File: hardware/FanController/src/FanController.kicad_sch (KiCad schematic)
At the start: 11 parts, among them J1 Conn_01x02_Socket, J2 Fan_4pin, J3 Fan_4pin, J4 Fan_4pin, J5 Fan_4pin, U1 PIC12F1501-xMC, U2 MCP9700Ax-ETT

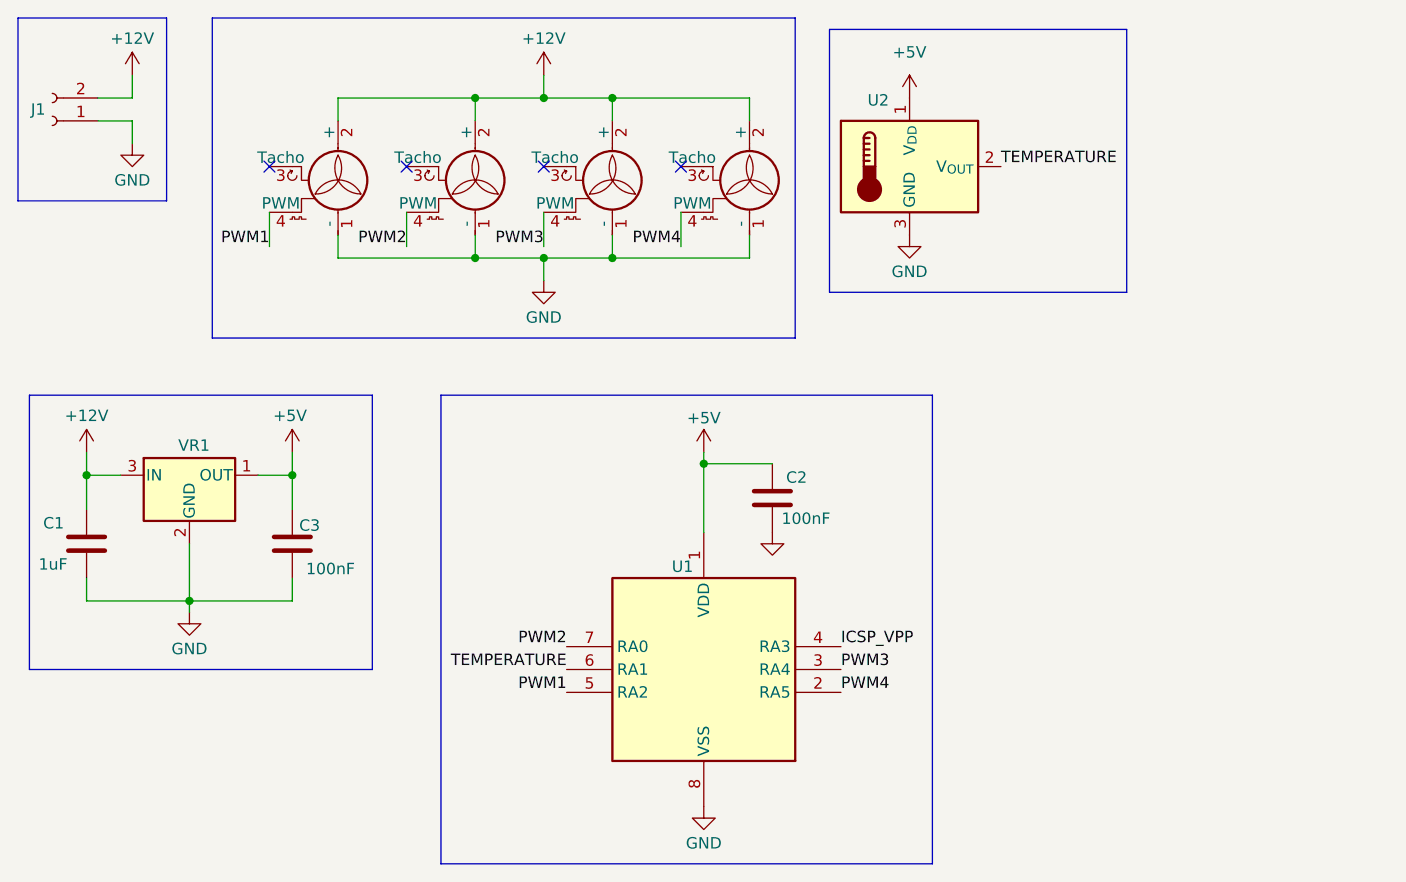
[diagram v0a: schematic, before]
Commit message: Replaced MCP9700A with MCP9701A
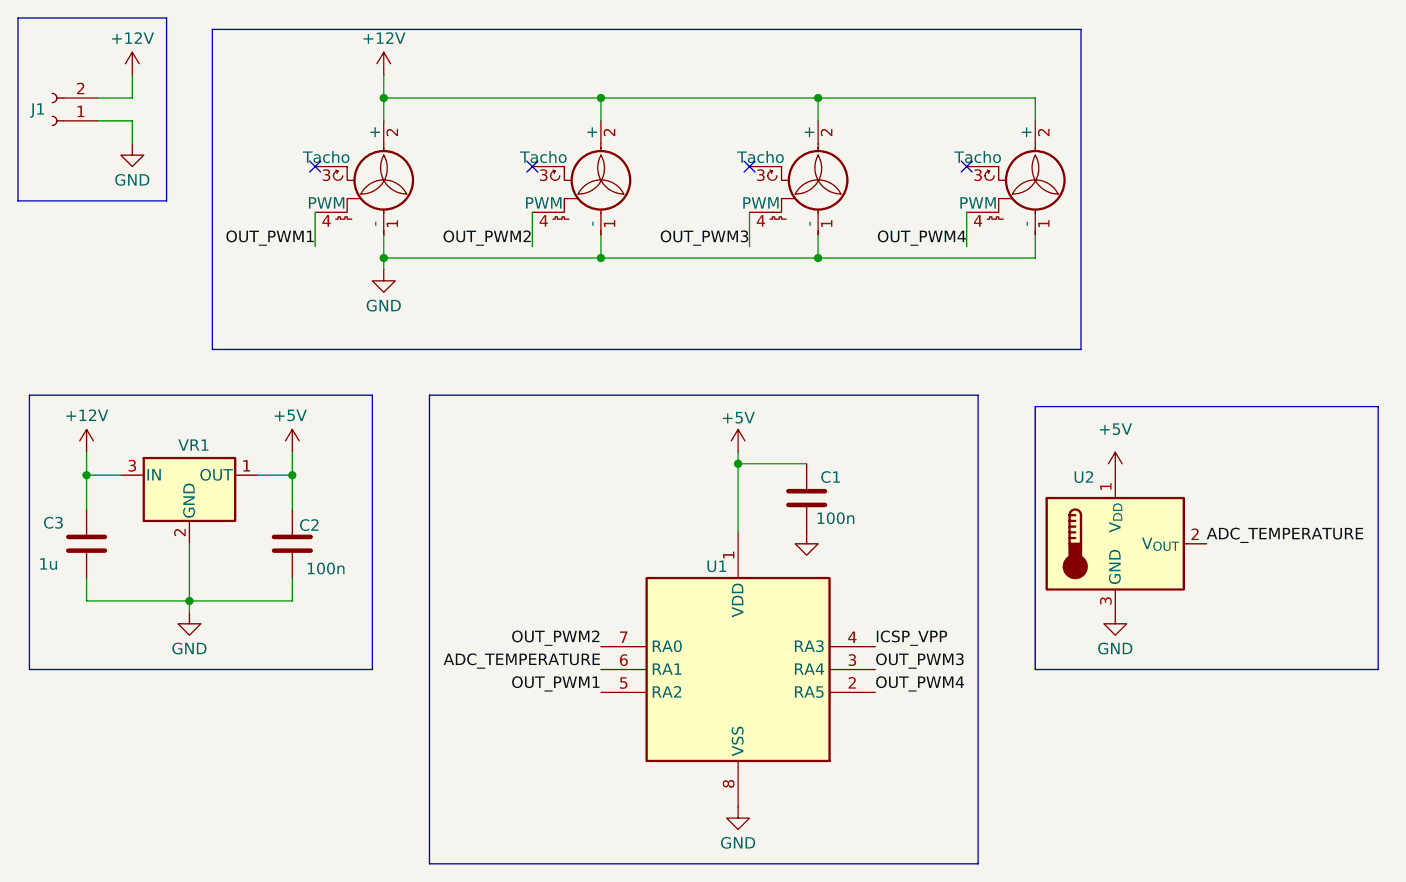
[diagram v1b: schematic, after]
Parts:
- C1: renamed from C2; value 100nF -> 100n
- C2: renamed from C3; value 100nF -> 100n
- C3: renamed from C1; value 1uF -> 1u
- J1: value Conn_01x02_Socket -> (none)
- J2, J3, J4, J5: value Fan_4pin -> (none)
- U1: value PIC12F1501-xMC -> PIC12F1501
- U2: value MCP9700Ax-ETT -> MCP9701A
- VR1: value MC78L05_SOT89 -> AS78L05RTR
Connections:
- net PWM1 renamed OUT_PWM1
- net PWM2 renamed OUT_PWM2
- net PWM3 renamed OUT_PWM3
- net PWM4 renamed OUT_PWM4
- net TEMPERATURE renamed ADC_TEMPERATURE
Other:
- moved on the sheet: C1, U1, U2
